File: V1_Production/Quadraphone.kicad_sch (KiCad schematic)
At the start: 38 parts, among them J1 Conn_01x10_Male, J2 Conn_01x10_Male, J3 Conn_01x10_Male, J4 Conn_01x10_Male, J5 Eurorack_10_pin_power, U1 AMS1117-5.0, U14 LM4040DBZ-2.5, U3 MCP6002, U4 LM4040DBZ-5, U5 MCP6004, U8 4066

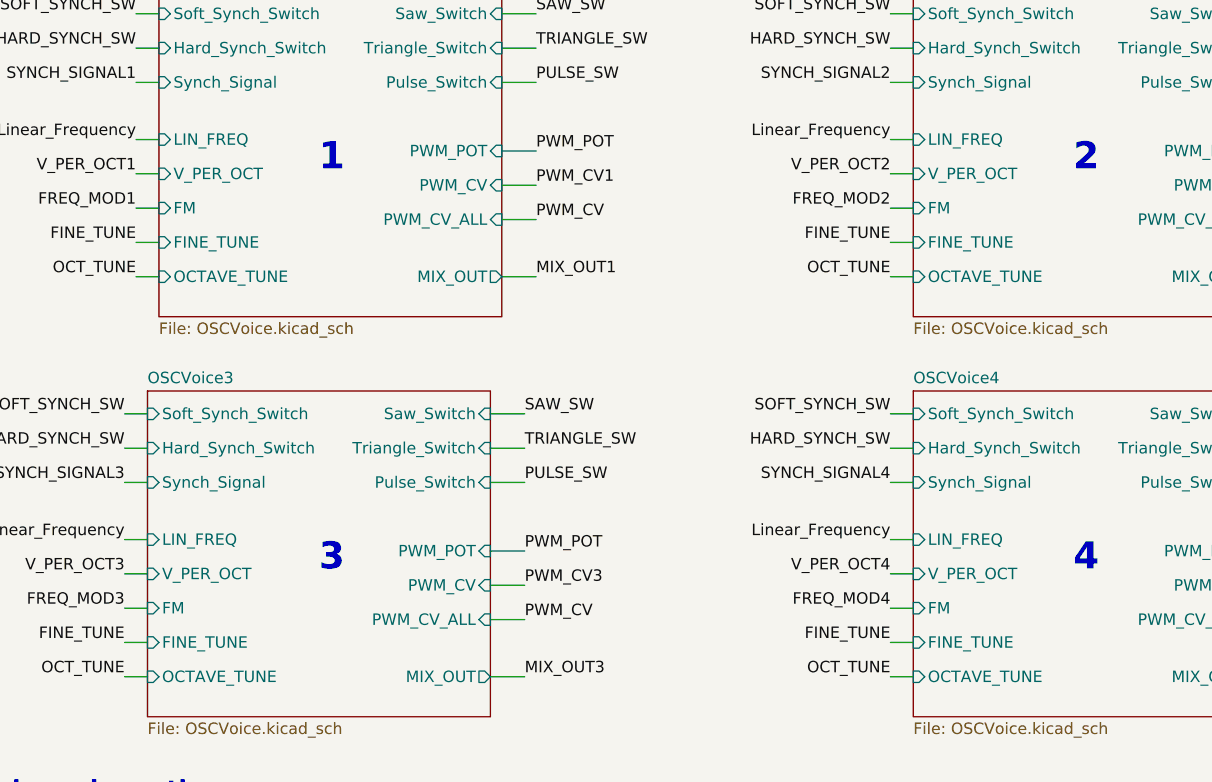
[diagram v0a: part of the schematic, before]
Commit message: Updates for v2 on control board
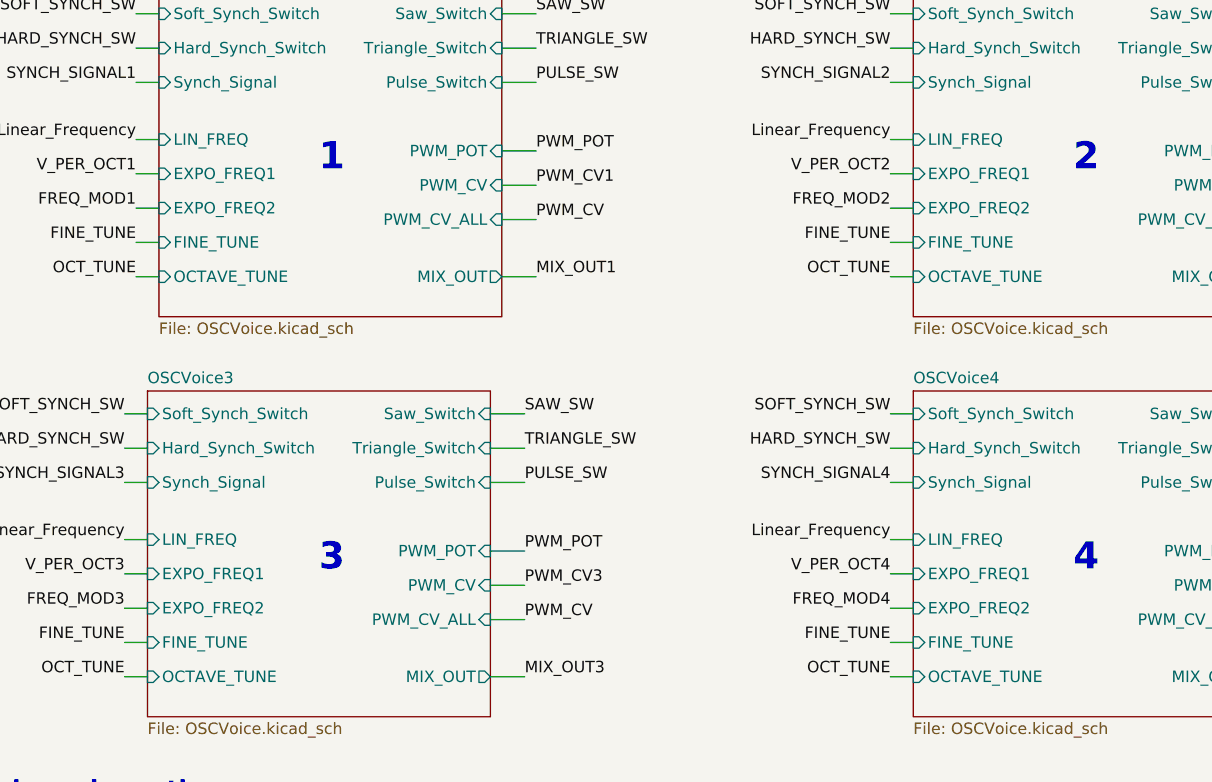
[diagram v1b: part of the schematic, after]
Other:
- sheet OSCVoice1 ports: added EXPO_FREQ1, EXPO_FREQ2; removed FM, V_PER_OCT
- sheet OSCVoice2 ports: added EXPO_FREQ1, EXPO_FREQ2; removed FM, V_PER_OCT
- sheet OSCVoice3 ports: added EXPO_FREQ1, EXPO_FREQ2; removed FM, V_PER_OCT
- sheet OSCVoice4 ports: added EXPO_FREQ1, EXPO_FREQ2; removed FM, V_PER_OCT
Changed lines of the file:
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@@
       (effects (font (size 1.27 1.27)) (justify left top))
     )
+    (pin "EXPO_FREQ1" input (at 36.83 40.64 180)
+      (effects (font (size 1.27 1.27)) (justify left))
+    )
     (pin "LIN_FREQ" input (at 36.83 36.83 180)
       (effects (font (size 1.27 1.27)) (justify left))
     )
+    (pin "EXPO_FREQ2" input (at 36.83 44.45 180)
+      (effects (font (size 1.27 1.27)) (justify left))
+    )
     (pin "MIX_OUT" output (at 74.93 52.07 0)
       (effects (font (size 1.27 1.27)) (justify right))
@@
     )
     (pin "FINE_TUNE" input (at 36.83 48.26 180)
-      (effects (font (size 1.27 1.27)) (justify left))
-    )
-    (pin "V_PER_OCT" input (at 36.83 40.64 180)
-      (effects (font (size 1.27 1.27)) (justify left))
-    )
-    (pin "FM" input (at 36.83 44.45 180)
       (effects (font (size 1.27 1.27)) (justify left))
     )
@@
       (effects (font (size 1.27 1.27)) (justify left top))
     )
+    (pin "EXPO_FREQ1" input (at 120.65 85.09 180)
+      (effects (font (size 1.27 1.27)) (justify left))
+    )
     (pin "LIN_FREQ" input (at 120.65 81.28 180)
       (effects (font (size 1.27 1.27)) (justify left))
     )
+    (pin "EXPO_FREQ2" input (at 120.65 88.9 180)
+      (effects (font (size 1.27 1.27)) (justify left))
+    )
     (pin "MIX_OUT" output (at 158.75 96.52 0)
       (effects (font (size 1.27 1.27)) (justify right))
@@
     )
     (pin "FINE_TUNE" input (at 120.65 92.71 180)
-      (effects (font (size 1.27 1.27)) (justify left))
-    )
-    (pin "V_PER_OCT" input (at 120.65 85.09 180)
-      (effects (font (size 1.27 1.27)) (justify left))
-    )
-    (pin "FM" input (at 120.65 88.9 180)
       (effects (font (size 1.27 1.27)) (justify left))
     )
@@
       (effects (font (size 1.27 1.27)) (justify left top))
     )
+    (pin "EXPO_FREQ1" input (at 35.56 85.09 180)
+      (effects (font (size 1.27 1.27)) (justify left))
+    )
     (pin "LIN_FREQ" input (at 35.56 81.28 180)
       (effects (font (size 1.27 1.27)) (justify left))
     )
+    (pin "EXPO_FREQ2" input (at 35.56 88.9 180)
+      (effects (font (size 1.27 1.27)) (justify left))
+    )
     (pin "MIX_OUT" output (at 73.66 96.52 0)
       (effects (font (size 1.27 1.27)) (justify right))
@@
     )
     (pin "FINE_TUNE" input (at 35.56 92.71 180)
-      (effects (font (size 1.27 1.27)) (justify left))
-    )
-    (pin "V_PER_OCT" input (at 35.56 85.09 180)
-      (effects (font (size 1.27 1.27)) (justify left))
-    )
-    (pin "FM" input (at 35.56 88.9 180)
       (effects (font (size 1.27 1.27)) (justify left))
     )
@@
       (effects (font (size 1.27 1.27)) (justify left top))
     )
+    (pin "EXPO_FREQ1" input (at 120.65 40.64 180)
+      (effects (font (size 1.27 1.27)) (justify left))
+    )
     (pin "LIN_FREQ" input (at 120.65 36.83 180)
       (effects (font (size 1.27 1.27)) (justify left))
     )
+    (pin "EXPO_FREQ2" input (at 120.65 44.45 180)
+      (effects (font (size 1.27 1.27)) (justify left))
+    )
     (pin "MIX_OUT" output (at 158.75 52.07 0)
       (effects (font (size 1.27 1.27)) (justify right))
@@
     )
     (pin "FINE_TUNE" input (at 120.65 48.26 180)
-      (effects (font (size 1.27 1.27)) (justify left))
-    )
-    (pin "V_PER_OCT" input (at 120.65 40.64 180)
-      (effects (font (size 1.27 1.27)) (justify left))
-    )
-    (pin "FM" input (at 120.65 44.45 180)
       (effects (font (size 1.27 1.27)) (justify left))
     )
@@
     )
     (path "/07c473a3-19f8-4492-9997-b494b1996c87/d75b5cc4-c26f-4cef-9931-cbdf165a8356"
-      (reference "R17") (unit 1) (value "680k") (footprint "Resistor_SMD:R_0603_1608Metric")
+      (reference "R17") (unit 1) (value "100k") (footprint "Resistor_SMD:R_0603_1608Metric")
     )
     (path "/07c473a3-19f8-4492-9997-b494b1996c87/692c6d62-f338-4339-acb3-e7feda895078"
@@
     )
     (path "/07c473a3-19f8-4492-9997-b494b1996c87/9a8af2a0-0d38-45ba-a477-4debc86730e5"
-      (reference "R22") (unit 1) (value "68k") (footprint "Resistor_SMD:R_0603_1608Metric")
+      (reference "R22") (unit 1) (value "49.9k") (footprint "Resistor_SMD:R_0603_1608Metric")
     )
     (path "/07c473a3-19f8-4492-9997-b494b1996c87/60b29eda-420b-486a-a1ff-8025e17bd651"
@@
     )
     (path "/61a45bbe-3c79-4a58-ba60-939f33076f4c/d75b5cc4-c26f-4cef-9931-cbdf165a8356"
-      (reference "R39") (unit 1) (value "680k") (footprint "Resistor_SMD:R_0603_1608Metric")
+      (reference "R39") (unit 1) (value "100k") (footprint "Resistor_SMD:R_0603_1608Metric")
     )
     (path "/61a45bbe-3c79-4a58-ba60-939f33076f4c/b2215372-f691-48bc-84a2-60658364ac9b"
@@
     )
     (path "/61a45bbe-3c79-4a58-ba60-939f33076f4c/9a8af2a0-0d38-45ba-a477-4debc86730e5"
-      (reference "R41") (unit 1) (value "68k") (footprint "Resistor_SMD:R_0603_1608Metric")
+      (reference "R41") (unit 1) (value "49.9k") (footprint "Resistor_SMD:R_0603_1608Metric")
     )
     (path "/61a45bbe-3c79-4a58-ba60-939f33076f4c/891b531b-bc5c-4886-831f-426632aea6dc"
@@
     )
     (path "/3fb79cf5-5f43-45eb-8dbe-e7a5213293f8/d75b5cc4-c26f-4cef-9931-cbdf165a8356"
-      (reference "R62") (unit 1) (value "680k") (footprint "Resistor_SMD:R_0603_1608Metric")
+      (reference "R62") (unit 1) (value "100k") (footprint "Resistor_SMD:R_0603_1608Metric")
     )
     (path "/3fb79cf5-5f43-45eb-8dbe-e7a5213293f8/b2215372-f691-48bc-84a2-60658364ac9b"
@@
     )
     (path "/3fb79cf5-5f43-45eb-8dbe-e7a5213293f8/9a8af2a0-0d38-45ba-a477-4debc86730e5"
-      (reference "R64") (unit 1) (value "68k") (footprint "Resistor_SMD:R_0603_1608Metric")
+      (reference "R64") (unit 1) (value "49.9k") (footprint "Resistor_SMD:R_0603_1608Metric")
     )
     (path "/3fb79cf5-5f43-45eb-8dbe-e7a5213293f8/891b531b-bc5c-4886-831f-426632aea6dc"
@@
     )
     (path "/5a2c2170-f030-4256-a64a-16cf3de949f5/d75b5cc4-c26f-4cef-9931-cbdf165a8356"
-      (reference "R85") (unit 1) (value "680k") (footprint "Resistor_SMD:R_0603_1608Metric")
+      (reference "R85") (unit 1) (value "100k") (footprint "Resistor_SMD:R_0603_1608Metric")
     )
     (path "/5a2c2170-f030-4256-a64a-16cf3de949f5/b2215372-f691-48bc-84a2-60658364ac9b"
@@
     )
     (path "/5a2c2170-f030-4256-a64a-16cf3de949f5/9a8af2a0-0d38-45ba-a477-4debc86730e5"
-      (reference "R87") (unit 1) (value "68k") (footprint "Resistor_SMD:R_0603_1608Metric")
+      (reference "R87") (unit 1) (value "49.9k") (footprint "Resistor_SMD:R_0603_1608Metric")
     )
     (path "/5a2c2170-f030-4256-a64a-16cf3de949f5/891b531b-bc5c-4886-831f-426632aea6dc"
